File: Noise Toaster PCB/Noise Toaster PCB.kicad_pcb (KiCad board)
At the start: 2 copper layers, 132.1 x 68.6 mm, 137 parts, among them J2 Power, J3 AREG, J4 LFO, J5 VCO, J6 VCO, J7 VCLPF, J8 VCA, J9 Amp, Q1 2N5457, Q10 2N3906, Q2 2N3904, Q3 2N3904, Q4 2N3904, Q5 2N3904, Q6 2N3904, Q7 2N5457, Q8 2N5457, Q9 2N5457, U1 LM324, U2 LM324, U3 LM386, X4 WNS

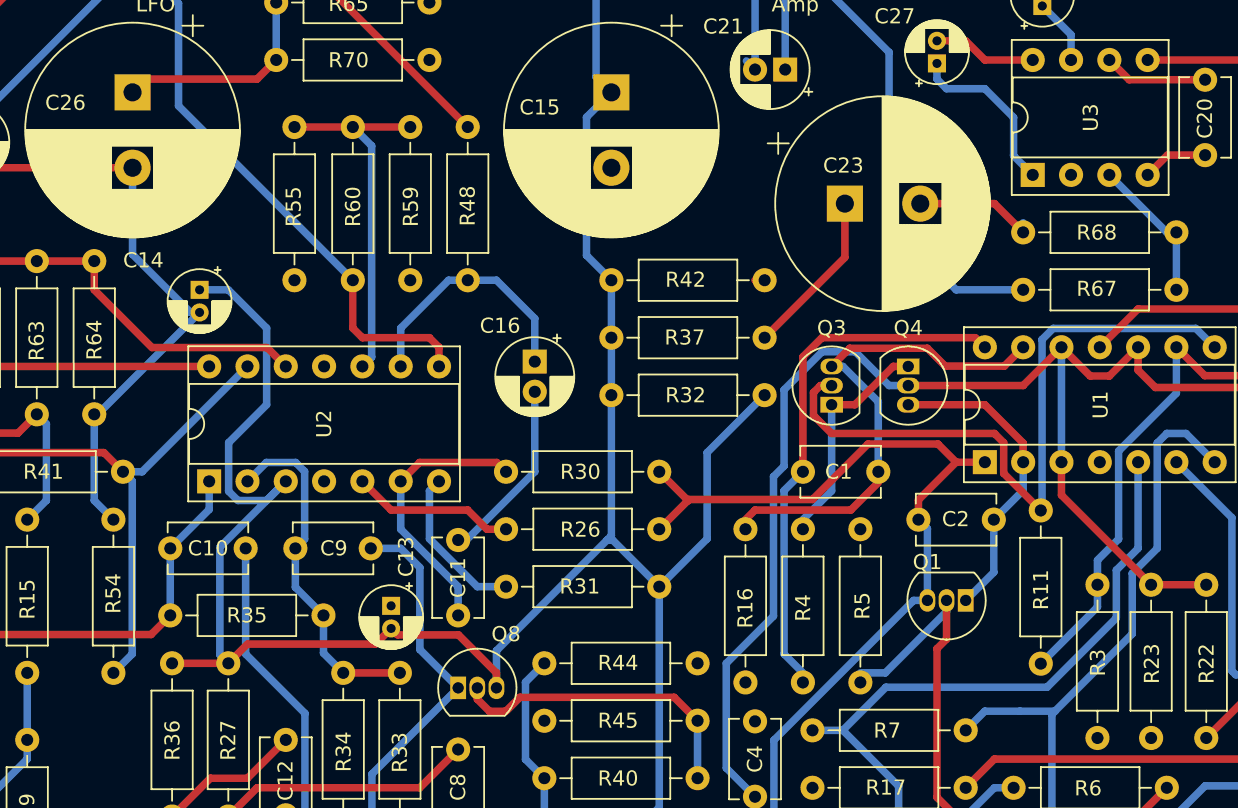
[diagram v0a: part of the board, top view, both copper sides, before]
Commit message: fixed silkscreen layer
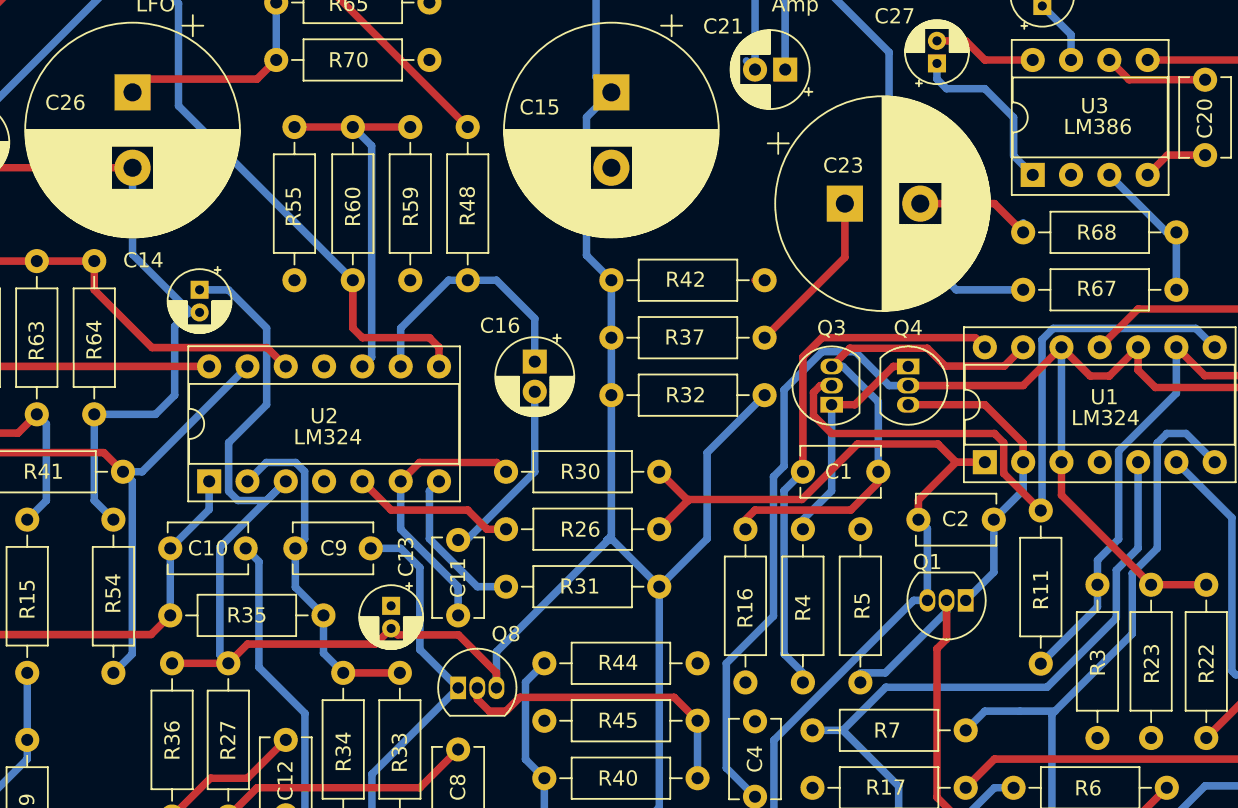
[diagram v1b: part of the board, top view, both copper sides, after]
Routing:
- net B-: track 126.8 -> 129.5 mm

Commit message: fixed minor issues with the pcb
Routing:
- net Net-(U2A--): track 23.2 -> 19.1 mm
- net GND: track 156.4 -> 158.2 mm
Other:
- board text added: "Experiments"
- board text added: "Music From Outer Space LLC Design by Ray Wilson CC-BY-NC-SA Rev 0.6.1"
- board text added: "Optional"
- board text removed: "Music From Outer Space LLC Design by Ray Wilson CC-BY-NC-SA Rev 0.6"
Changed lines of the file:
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@@
   (title_block
     (title "Noise Toaster")
-    (date "2023-09-13")
-    (rev "0.6")
+    (date "2023-10-29")
+    (rev "0.6.1")
     (company "Music From Outer Space LLC")
     (comment 1 "Licence: CC-BY-NC-SA")
@@
     (property "ki_keywords" "cap capacitor")
     (attr through_hole)
-    (fp_text reference "C27" (at 3.1226 -2.8 180) (layer "F.SilkS")
+    (fp_text reference "C27" (at 3.405 -2.286 180) (layer "F.SilkS")
         (effects (font (size 1 1) (thickness 0.15)))
     )
@@
     )
   )
+  (gr_rect (start 162.972 80.926) (end 170.338 87.276)
+    (stroke (width 0.15) (type dash)) (fill none) (layer "F.SilkS"))
+  (gr_rect (start 195.23 88.8) (end 206.406 105.056)
+    (stroke (width 0.15) (type dash_dot_dot)) (fill none) (layer "F.SilkS"))
   (gr_rect (start 75.271 75.267) (end 207.351 143.847)
     (stroke (width 0.2) (type default)) (fill none) (layer "Edge.Cuts"))
@@
     (effects (font (size 1.27 1.27) (thickness 0.15)))
   )
-  (gr_text "Music From Outer Space LLC\nDesign by Ray Wilson\nCC-BY-NC-SA\nRev 0.6" (at 176.942 142.648) (layer "F.SilkS")
+  (gr_text "Music From Outer Space LLC\nDesign by Ray Wilson\nCC-BY-NC-SA\nRev 0.6.1" (at 176.942 142.648) (layer "F.SilkS")
     (effects (font (size 1 1) (thickness 0.15)) (justify left bottom))
   )
@@
     (effects (font (size 1.27 1.27) (thickness 0.15)))
   )
+  (gr_text "Experiments" (at 197.262 106.58) (layer "F.SilkS")
+    (effects (font (size 1 1) (thickness 0.15)) (justify left bottom))
+  )
   (gr_text "Noise Toaster" (at 85.301 78.767) (layer "F.SilkS")
     (effects (font (size 2 2) (thickness 0.15)) (justify left bottom))
@@
     (effects (font (size 1.27 1.27) (thickness 0.15)))
   )
+  (gr_text "Optional" (at 163.734 80.418) (layer "F.SilkS")
+    (effects (font (size 1 1) (thickness 0.15)) (justify left bottom))
+  )
   (gr_text "" (at 199.548 100.738) (layer "F.SilkS")
     (effects (font (size 1.27 1.27) (thickness 0.15)))
@@
   (segment (start 132.746 124.212) (end 135.286 126.752) (width 0.5) (layer "B.Cu") (net 16))
   (segment (start 131.421 125.757) (end 127.666 125.757) (width 0.5) (layer "F.Cu") (net 17))
-  (segment (start 125.106 112.402) (end 124.511 111.807) (width 0.5) (layer "B.Cu") (net 17))
+  (segment (start 121.316 114.327) (end 124.491 117.502) (width 0.5) (layer "B.Cu") (net 17))
   (segment (start 124.491 120.082) (end 126.356 121.947) (width 0.5) (layer "B.Cu") (net 17))
-  (segment (start 124.491 117.502) (end 125.106 116.887) (width 0.5) (layer "B.Cu") (net 17))
-  (segment (start 125.106 116.887) (end 125.106 112.402) (width 0.5) (layer "B.Cu") (net 17))
-  (segment (start 124.511 111.807) (end 122.566 111.807) (width 0.5) (layer "B.Cu") (net 17))
-  (segment (start 122.566 111.807) (end 121.316 113.057) (width 0.5) (layer "B.Cu") (net 17))
+  (segment (start 121.316 113.057) (end 121.316 114.327) (width 0.5) (layer "B.Cu") (net 17))
   (segment (start 126.356 124.447) (end 127.666 125.757) (width 0.5) (layer "B.Cu") (net 17))
   (segment (start 124.491 117.502) (end 124.491 120.082) (width 0.5) (layer "B.Cu") (net 17))
@@
   (segment (start 145.446 99.722) (end 145.446 103.532) (width 0.5) (layer "B.Cu") (net 23))
   (segment (start 151.796 111.152) (end 151.796 116.867) (width 0.5) (layer "B.Cu") (net 23))
-  (segment (start 119.483871 124.559871) (end 120.046 125.122) (width 0.5) (layer "B.Cu") (net 23))
   (segment (start 148.621 134.679) (end 143.192 140.108) (width 0.5) (layer "B.Cu") (net 23))
   (segment (start 143.796 98.072) (end 145.446 99.722) (width 0.5) (layer "B.Cu") (net 23))
-  (segment (start 120.046 100.357) (end 122.586 102.897) (width 0.5) (layer "B.Cu") (net 23))
-  (segment (start 120.066 113.712) (end 120.681 114.327) (width 0.5) (layer "B.Cu") (net 23))
-  (segment (start 122.586 107.977) (end 120.066 110.497) (width 0.5) (layer "B.Cu") (net 23))
+  (segment (start 121.189 100.357) (end 125.106 104.274) (width 0.5) (layer "B.Cu") (net 23))
   (segment (start 144.43 86.248272) (end 145.446 87.264272) (width 0.5) (layer "B.Cu") (net 23))
   (segment (start 145.446 87.264272) (end 143.796 88.914272) (width 0.5) (layer "B.Cu") (net 23))
-  (segment (start 118.141 100.357) (end 120.046 100.357) (width 0.5) (layer "B.Cu") (net 23))
   (segment (start 145.446 107.342) (end 145.446 116.663224) (width 0.5) (layer "B.Cu") (net 23))
+  (segment (start 119.284 125.122) (end 120.046 125.122) (width 0.5) (layer "B.Cu") (net 23))
   (segment (start 155.606 107.342) (end 151.796 111.152) (width 0.5) (layer "B.Cu") (net 23))
-  (segment (start 120.681 114.327) (end 122.586 114.327) (width 0.5) (layer "B.Cu") (net 23))
   (segment (start 148.621 120.042) (end 148.621 134.679) (width 0.5) (layer "B.Cu") (net 23))
   (segment (start 145.534612 116.955612) (end 145.153612 116.955612) (width 0.5) (layer "B.Cu") (net 23))
   (segment (start 145.446 116.663224) (end 145.153612 116.955612) (width 0.5) (layer "B.Cu") (net 23))
-  (segment (start 123.221 113.692) (end 119.483871 117.429129) (width 0.5) (layer "B.Cu") (net 23))
+  (segment (start 123.856 113.057) (end 122.439 111.64) (width 0.5) (layer "B.Cu") (net 23))
+  (segment (start 120.066 111.64) (end 120.066 115.744) (width 0.5) (layer "B.Cu") (net 23))
   (segment (start 137.826 124.36) (end 137.826 126.752) (width 0.5) (layer "B.Cu") (net 23))
-  (segment (start 122.586 114.327) (end 123.221 113.692) (width 0.5) (layer "B.Cu") (net 23))
   (segment (start 145.446 107.342) (end 145.446 103.532) (width 0.5) (layer "B.Cu") (net 23))
+  (segment (start 120.066 115.744) (end 119.284 116.526) (width 0.5) (layer "B.Cu") (net 23))
   (segment (start 143.796 88.914272) (end 143.796 98.072) (width 0.5) (layer "B.Cu") (net 23))
   (segment (start 144.43 79.148) (end 144.43 86.248272) (width 0.5) (layer "B.Cu") (net 23))
-  (segment (start 122.586 102.897) (end 122.586 107.977) (width 0.5) (layer "B.Cu") (net 23))
   (segment (start 145.153612 116.955612) (end 145.153612 117.032388) (width 0.5) (layer "B.Cu") (net 23))
-  (segment (start 120.066 110.497) (end 120.066 113.712) (width 0.5) (layer "B.Cu") (net 23))
-  (segment (start 123.221 113.692) (end 123.856 113.057) (width 0.5) (layer "B.Cu") (net 23))
   (segment (start 145.153612 117.032388) (end 137.826 124.36) (width 0.5) (layer "B.Cu") (net 23))
+  (segment (start 119.284 116.526) (end 119.284 125.122) (width 0.5) (layer "B.Cu") (net 23))
   (segment (start 148.621 120.042) (end 145.534612 116.955612) (width 0.5) (layer "B.Cu") (net 23))
+  (segment (start 125.106 104.274) (end 125.106 106.6) (width 0.5) (layer "B.Cu") (net 23))
+  (segment (start 122.439 111.64) (end 120.066 111.64) (width 0.5) (layer "B.Cu") (net 23))
+  (segment (start 125.106 106.6) (end 120.066 111.64) (width 0.5) (layer "B.Cu") (net 23))
+  (segment (start 118.141 100.357) (end 121.189 100.357) (width 0.5) (layer "B.Cu") (net 23))
   (segment (start 151.796 116.867) (end 148.621 120.042) (width 0.5) (layer "B.Cu") (net 23))
-  (segment (start 119.483871 117.429129) (end 119.483871 124.559871) (width 0.5) (layer "B.Cu") (net 23))
   (segment (start 140.366 102.262) (end 140.366 105.116888) (width 0.5) (layer "B.Cu") (net 24))
   (segment (start 135.921 99.722) (end 137.826 99.722) (width 0.5) (layer "B.Cu") (net 24))
